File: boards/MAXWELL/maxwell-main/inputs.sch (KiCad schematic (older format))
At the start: 1 part, among them U4 XC7S6-1FTGB196C

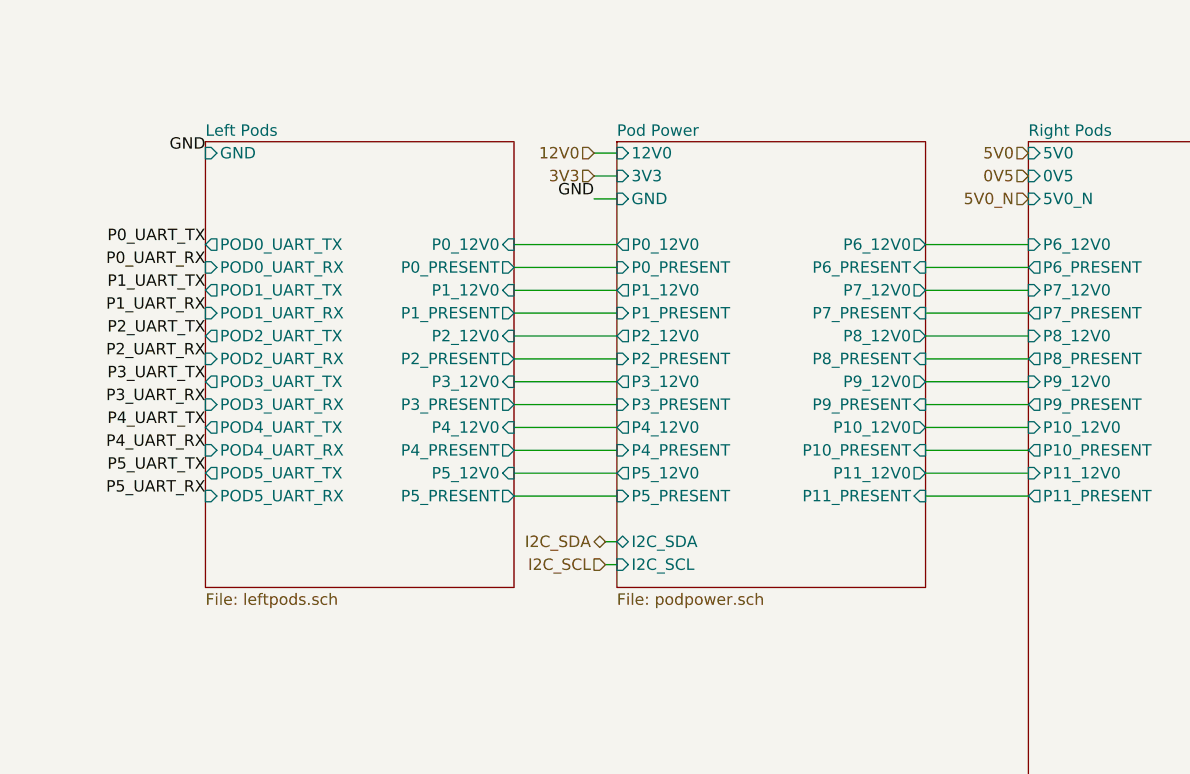
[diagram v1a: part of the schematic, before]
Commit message: Added ferrites to 12V power outputs to improve EMC performance. Fixed incorrect 1V0 hookup for small FPGA. Fixed some other ERC errors
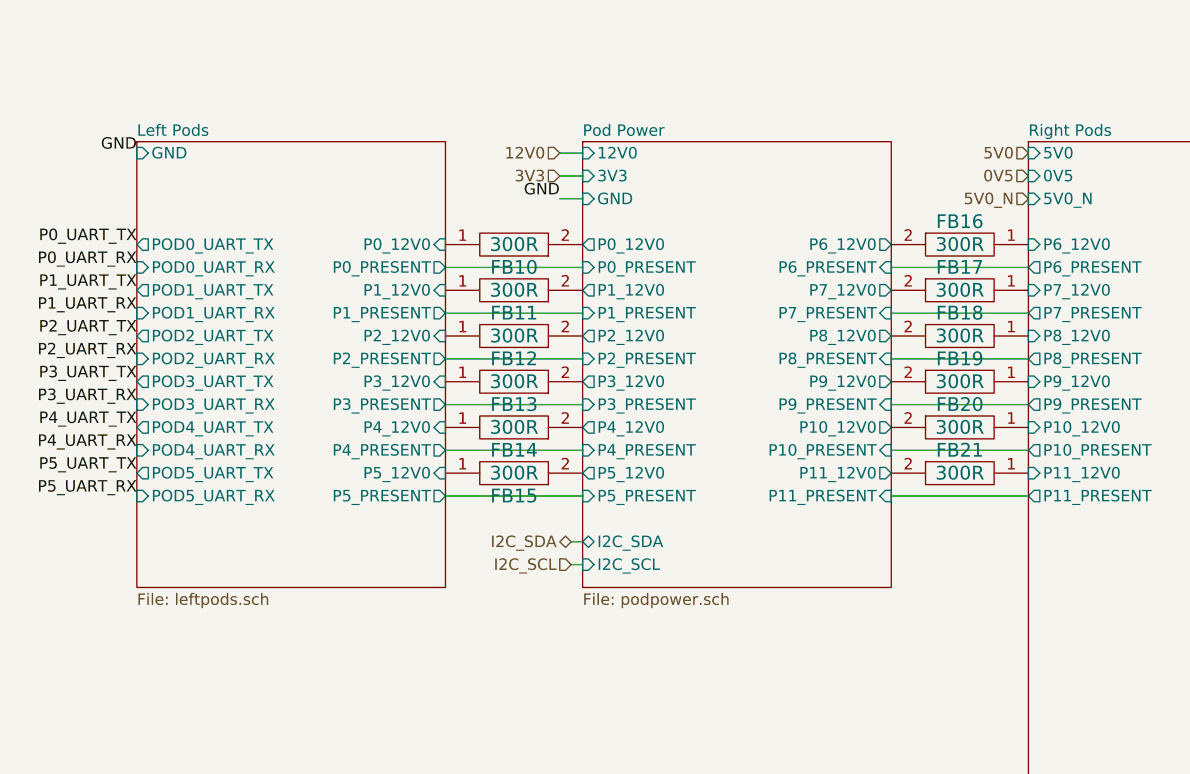
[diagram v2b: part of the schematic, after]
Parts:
- added FB10, FB11, FB12, FB13, FB14, FB15, FB16, FB17, FB18, FB19, FB20, FB21: 300R, symbol passive-azonenberg:FERRITE_SMALL
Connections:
- net Left Pods/P0_12V0: now also FB10.1
- net Left Pods/P1_12V0: now also FB11.1
- net Left Pods/P2_12V0: now also FB12.1
- net Left Pods/P3_12V0: now also FB13.1
- net Left Pods/P4_12V0: now also FB14.1
- net Left Pods/P5_12V0: now also FB15.1
- net Pod Power/P10_12V0: now also FB20.2
- net Pod Power/P11_12V0: now also FB21.2
- net Pod Power/P6_12V0: now also FB16.2
- net Pod Power/P7_12V0: now also FB17.2
- net Pod Power/P8_12V0: now also FB18.2
- net Pod Power/P9_12V0: now also FB19.2
- new net Pod Power/P0_12V0: FB10.2
- new net Pod Power/P1_12V0: FB11.2
- new net Pod Power/P2_12V0: FB12.2
- new net Pod Power/P3_12V0: FB13.2
- new net Pod Power/P4_12V0: FB14.2
- new net Pod Power/P5_12V0: FB15.2
- new net Right Pods/P10_12V0: FB20.1
- new net Right Pods/P11_12V0: FB21.1
- new net Right Pods/P6_12V0: FB16.1
- new net Right Pods/P7_12V0: FB17.1
- new net Right Pods/P8_12V0: FB18.1
- new net Right Pods/P9_12V0: FB19.1

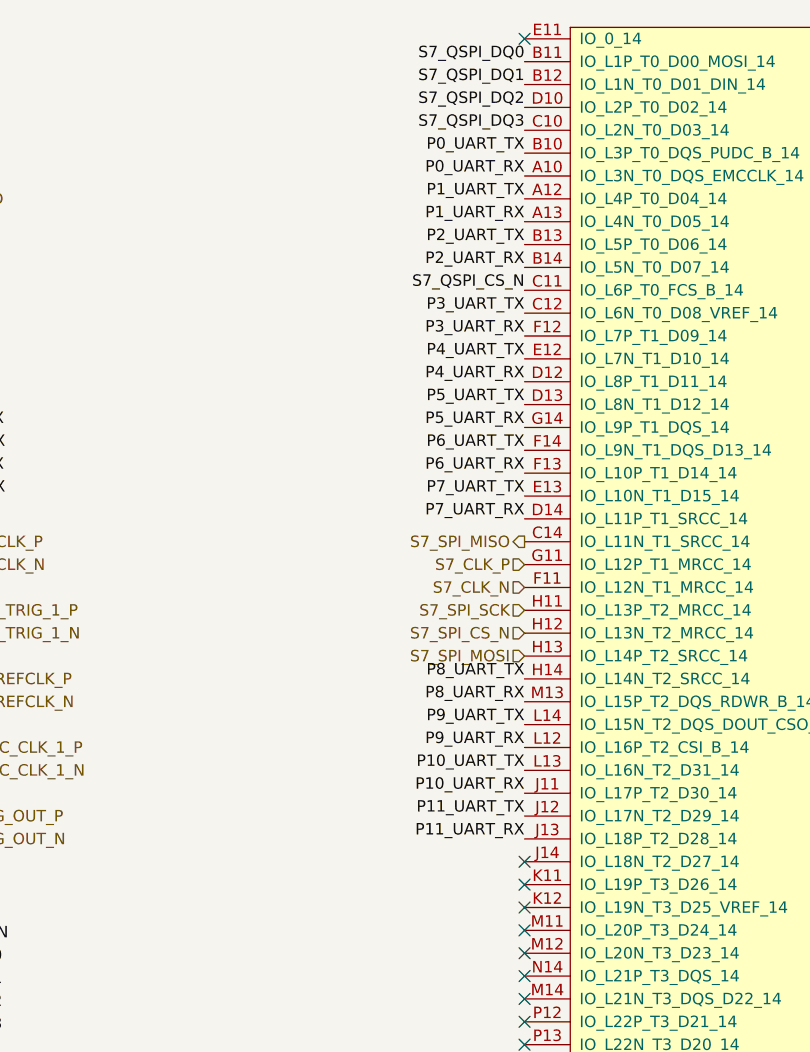
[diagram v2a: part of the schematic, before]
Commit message: Added missing PUDC_B pullup resistors
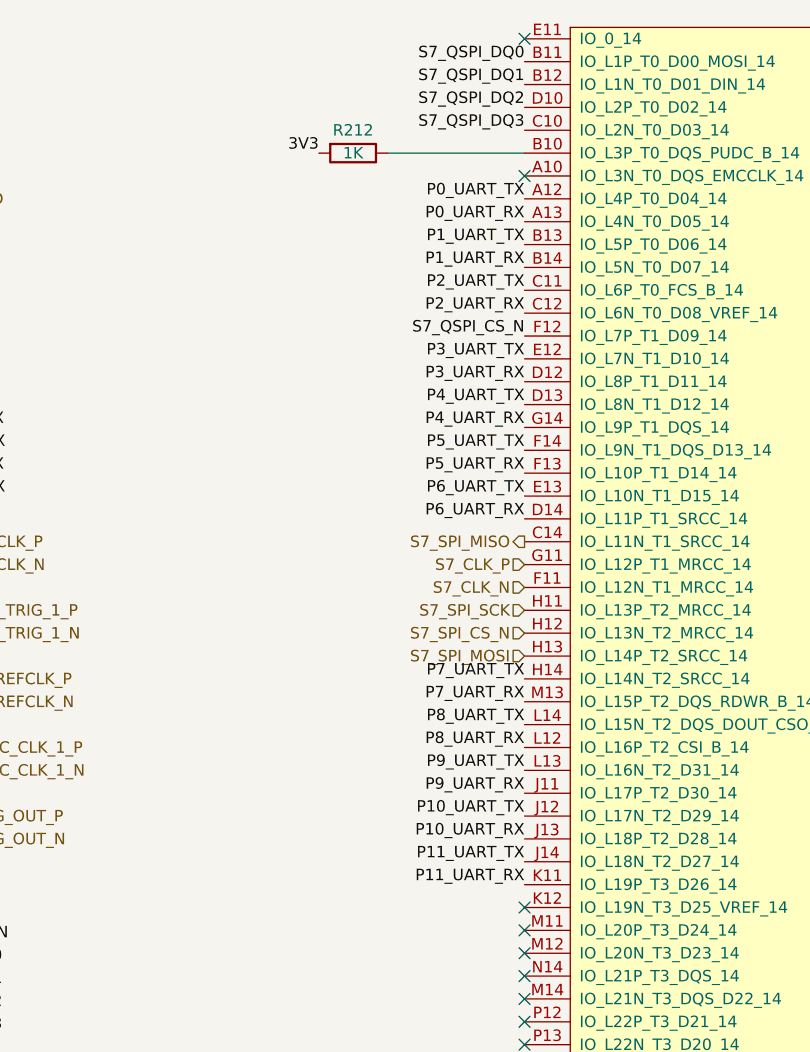
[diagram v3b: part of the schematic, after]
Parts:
- added R212: 1K, symbol device:R
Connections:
- net 3V3: now also R212.2
- net P0_UART_RX: now also U4.A13 (IO_L4N_T0_D05_14); no longer U4.A10 (IO_L3N_T0_DQS_EMCCLK_14)
- net P0_UART_TX: now also U4.A12 (IO_L4P_T0_D04_14); no longer U4.B10 (IO_L3P_T0_DQS_PUDC_B_14)
- net P10_UART_RX: now also U4.J13 (IO_L18P_T2_D28_14); no longer U4.J11 (IO_L17P_T2_D30_14)
- net P10_UART_TX: now also U4.J12 (IO_L17N_T2_D29_14); no longer U4.L13 (IO_L16N_T2_D31_14)
- net P11_UART_RX: now also U4.K11 (IO_L19P_T3_D26_14); no longer U4.J13 (IO_L18P_T2_D28_14)
- net P11_UART_TX: now also U4.J14 (IO_L18N_T2_D27_14); no longer U4.J12 (IO_L17N_T2_D29_14)
- net P1_UART_RX: now also U4.B14 (IO_L5N_T0_D07_14); no longer U4.A13 (IO_L4N_T0_D05_14)
- net P1_UART_TX: now also U4.B13 (IO_L5P_T0_D06_14); no longer U4.A12 (IO_L4P_T0_D04_14)
- net P2_UART_RX: now also U4.C12 (IO_L6N_T0_D08_VREF_14); no longer U4.B14 (IO_L5N_T0_D07_14)
- net P2_UART_TX: now also U4.C11 (IO_L6P_T0_FCS_B_14); no longer U4.B13 (IO_L5P_T0_D06_14)
- net P3_UART_RX: now also U4.D12 (IO_L8P_T1_D11_14); no longer U4.F12 (IO_L7P_T1_D09_14)
- net P3_UART_TX: now also U4.E12 (IO_L7N_T1_D10_14); no longer U4.C12 (IO_L6N_T0_D08_VREF_14)
- net P4_UART_RX: now also U4.G14 (IO_L9P_T1_DQS_14); no longer U4.D12 (IO_L8P_T1_D11_14)
- net P4_UART_TX: now also U4.D13 (IO_L8N_T1_D12_14); no longer U4.E12 (IO_L7N_T1_D10_14)
- net P5_UART_RX: now also U4.F13 (IO_L10P_T1_D14_14); no longer U4.G14 (IO_L9P_T1_DQS_14)
- net P5_UART_TX: now also U4.F14 (IO_L9N_T1_DQS_D13_14); no longer U4.D13 (IO_L8N_T1_D12_14)
- net P6_UART_RX: now also U4.D14 (IO_L11P_T1_SRCC_14); no longer U4.F13 (IO_L10P_T1_D14_14)
- net P6_UART_TX: now also U4.E13 (IO_L10N_T1_D15_14); no longer U4.F14 (IO_L9N_T1_DQS_D13_14)
- net P7_UART_RX: now also U4.M13 (IO_L15P_T2_DQS_RDWR_B_14); no longer U4.D14 (IO_L11P_T1_SRCC_14)
- net P7_UART_TX: now also U4.H14 (IO_L14N_T2_SRCC_14); no longer U4.E13 (IO_L10N_T1_D15_14)
- net P8_UART_RX: now also U4.L12 (IO_L16P_T2_CSI_B_14); no longer U4.M13 (IO_L15P_T2_DQS_RDWR_B_14)
- net P8_UART_TX: now also U4.L14 (IO_L15N_T2_DQS_DOUT_CSO_B_14); no longer U4.H14 (IO_L14N_T2_SRCC_14)
- net P9_UART_RX: now also U4.J11 (IO_L17P_T2_D30_14); no longer U4.L12 (IO_L16P_T2_CSI_B_14)
- net P9_UART_TX: now also U4.L13 (IO_L16N_T2_D31_14); no longer U4.L14 (IO_L15N_T2_DQS_DOUT_CSO_B_14)
- net S7_QSPI_CS_N: now also U4.F12 (IO_L7P_T1_D09_14); no longer U4.C11 (IO_L6P_T0_FCS_B_14)
- new net: R212.1, U4.B10 (IO_L3P_T0_DQS_PUDC_B_14)
- no-connect marks 15 -> 14
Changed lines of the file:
@@
 Sheet 7 18
 Title "MAXWELL Main Board"
-Date "2020-06-21"
+Date "2020-06-22"
 Rev "0.1"
 Comp "Antikernel Labs"
@@
 F13 "S7_DONE" O L 5000 5500 50
 $EndSheet
-Text Label 9100 1950 2    50   ~ 0
+Text Label 9100 2150 2    50   ~ 0
 S7_QSPI_CS_N
 Text Label 9100 950  2    50   ~ 0
@@
 F43 "5V0_N" I L 5000 1550 50
 $EndSheet
-Text Label 9100 1350 2    50   ~ 0
+Text Label 9100 1550 2    50   ~ 0
 P0_UART_TX
-Text Label 9100 1450 2    50   ~ 0
+Text Label 9100 1650 2    50   ~ 0
 P0_UART_RX
 Text HLabel 9100 3150 0    50   Input ~ 0
@@
 Text HLabel 9100 3250 0    50   Input ~ 0
 S7_CLK_N
-Text Label 9100 1550 2    50   ~ 0
+Text Label 9100 1750 2    50   ~ 0
 P1_UART_TX
-Text Label 9100 1650 2    50   ~ 0
+Text Label 9100 1850 2    50   ~ 0
 P1_UART_RX
 Text HLabel 9100 3450 0    50   Input ~ 0
@@
 Text HLabel 9100 3050 0    50   Output ~ 0
 S7_SPI_MISO
-Text Label 9100 1750 2    50   ~ 0
+Text Label 9100 1950 2    50   ~ 0
 P2_UART_TX
-Text Label 9100 1850 2    50   ~ 0
+Text Label 9100 2050 2    50   ~ 0
 P2_UART_RX
-Text Label 9100 2050 2    50   ~ 0
+Text Label 9100 2250 2    50   ~ 0
 P3_UART_TX
-Text Label 9100 2150 2    50   ~ 0
+Text Label 9100 2350 2    50   ~ 0
 P3_UART_RX
-Text Label 9100 2250 2    50   ~ 0
+Text Label 9100 2450 2    50   ~ 0
 P4_UART_TX
-Text Label 9100 2350 2    50   ~ 0
+Text Label 9100 2550 2    50   ~ 0
 P4_UART_RX
-Text Label 9100 2450 2    50   ~ 0
+Text Label 9100 2650 2    50   ~ 0
 P5_UART_TX
-Text Label 9100 2550 2    50   ~ 0
+Text Label 9100 2750 2    50   ~ 0
 P5_UART_RX
-Text Label 9100 2650 2    50   ~ 0
+Text Label 9100 2850 2    50   ~ 0
 P6_UART_TX
-Text Label 9100 2750 2    50   ~ 0
+Text Label 9100 2950 2    50   ~ 0
 P6_UART_RX
-Text Label 9100 2850 2    50   ~ 0
+Text Label 9100 3650 2    50   ~ 0
 P7_UART_TX
-Text Label 9100 2950 2    50   ~ 0
+Text Label 9100 3750 2    50   ~ 0
 P7_UART_RX
-Text Label 9100 3650 2    50   ~ 0
+Text Label 9100 3850 2    50   ~ 0
 P8_UART_TX
-Text Label 9100 3750 2    50   ~ 0
+Text Label 9100 3950 2    50   ~ 0
 P8_UART_RX
-Text Label 9100 3850 2    50   ~ 0
+Text Label 9100 4050 2    50   ~ 0
 P9_UART_TX
-Text Label 9100 3950 2    50   ~ 0
+Text Label 9100 4150 2    50   ~ 0
 P9_UART_RX
-Text Label 9100 4050 2    50   ~ 0
+Text Label 9100 4250 2    50   ~ 0
 P10_UART_TX
-Text Label 9100 4150 2    50   ~ 0
+Text Label 9100 4350 2    50   ~ 0
 P10_UART_RX
-Text Label 9100 4250 2    50   ~ 0
+Text Label 9100 4450 2    50   ~ 0
 P11_UART_TX
-Text Label 9100 4350 2    50   ~ 0
+Text Label 9100 4550 2    50   ~ 0
 P11_UART_RX
 Text HLabel 6600 3050 2    50   Input ~ 0
@@
 NoConn ~ 9100 5750
 NoConn ~ 9100 850
-NoConn ~ 9100 4450
-NoConn ~ 9100 4550
 NoConn ~ 9100 4650
 NoConn ~ 9100 4750
@@
 	-1   0    0    1
 $EndComp
+NoConn ~ 9100 1450
+$Comp
+L device:R R212
+U 1 1 61DE8149
+P 8350 1350
+F 0 "R212" V 8250 1350 50  0000 C CNN
+F 1 "1K" V 8350 1350 50  0000 C CNN
+F 2 "" V 8280 1350 50  0001 C CNN
+F 3 "" H 8350 1350 50  0001 C CNN
+	1    8350 1350
+	0    1    1    0
+$EndComp
+Wire Wire Line
+	8500 1350 9100 1350
+Text Label 8200 1350 2    50   ~ 0
+3V3
 $EndSCHEMATC

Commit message: Continued schematic review. Finished verifying pinouts. Assigned lots more footprints.
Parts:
- FB10, FB11, FB12, FB13, FB14, FB15, FB16, FB17, FB18, FB19, FB20, FB21: footprint (none) -> azonenberg_pcb:EIA_2220_INDUCTOR
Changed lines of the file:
@@
 F 0 "FB11" H 2750 2050 60  0000 C CNN
 F 1 "300R" H 2750 1950 60  0000 C CNN
-F 2 "" H 2750 1950 60  0001 C CNN
+F 2 "azonenberg_pcb:EIA_2220_INDUCTOR" H 2750 1950 60  0001 C CNN
 F 3 "" H 2750 1950 60  0000 C CNN
 	1    2750 1950
@@
 F 0 "FB13" H 2750 2450 60  0000 C CNN
 F 1 "300R" H 2750 2350 60  0000 C CNN
-F 2 "" H 2750 2350 60  0001 C CNN
+F 2 "azonenberg_pcb:EIA_2220_INDUCTOR" H 2750 2350 60  0001 C CNN
 F 3 "" H 2750 2350 60  0000 C CNN
 	1    2750 2350
@@
 F 0 "FB14" H 2750 2650 60  0000 C CNN
 F 1 "300R" H 2750 2550 60  0000 C CNN
-F 2 "" H 2750 2550 60  0001 C CNN
+F 2 "azonenberg_pcb:EIA_2220_INDUCTOR" H 2750 2550 60  0001 C CNN
 F 3 "" H 2750 2550 60  0000 C CNN
 	1    2750 2550
@@
 F 0 "FB15" H 2750 2850 60  0000 C CNN
 F 1 "300R" H 2750 2750 60  0000 C CNN
-F 2 "" H 2750 2750 60  0001 C CNN
+F 2 "azonenberg_pcb:EIA_2220_INDUCTOR" H 2750 2750 60  0001 C CNN
 F 3 "" H 2750 2750 60  0000 C CNN
 	1    2750 2750
@@
 F 0 "FB16" H 4700 1850 60  0000 C CNN
 F 1 "300R" H 4700 1750 60  0000 C CNN
-F 2 "" H 4700 1750 60  0001 C CNN
+F 2 "azonenberg_pcb:EIA_2220_INDUCTOR" H 4700 1750 60  0001 C CNN
 F 3 "" H 4700 1750 60  0000 C CNN
 	1    4700 1750
@@
 F 0 "FB17" H 4700 2050 60  0000 C CNN
 F 1 "300R" H 4700 1950 60  0000 C CNN
-F 2 "" H 4700 1950 60  0001 C CNN
+F 2 "azonenberg_pcb:EIA_2220_INDUCTOR" H 4700 1950 60  0001 C CNN
 F 3 "" H 4700 1950 60  0000 C CNN
 	1    4700 1950
@@
 F 0 "FB18" H 4700 2250 60  0000 C CNN
 F 1 "300R" H 4700 2150 60  0000 C CNN
-F 2 "" H 4700 2150 60  0001 C CNN
+F 2 "azonenberg_pcb:EIA_2220_INDUCTOR" H 4700 2150 60  0001 C CNN
 F 3 "" H 4700 2150 60  0000 C CNN
 	1    4700 2150
@@
 F 0 "FB19" H 4700 2450 60  0000 C CNN
 F 1 "300R" H 4700 2350 60  0000 C CNN
-F 2 "" H 4700 2350 60  0001 C CNN
+F 2 "azonenberg_pcb:EIA_2220_INDUCTOR" H 4700 2350 60  0001 C CNN
 F 3 "" H 4700 2350 60  0000 C CNN
 	1    4700 2350
@@
 F 0 "FB20" H 4700 2650 60  0000 C CNN
 F 1 "300R" H 4700 2550 60  0000 C CNN
-F 2 "" H 4700 2550 60  0001 C CNN
+F 2 "azonenberg_pcb:EIA_2220_INDUCTOR" H 4700 2550 60  0001 C CNN
 F 3 "" H 4700 2550 60  0000 C CNN
 	1    4700 2550
@@
 F 0 "FB21" H 4700 2850 60  0000 C CNN
 F 1 "300R" H 4700 2750 60  0000 C CNN
-F 2 "" H 4700 2750 60  0001 C CNN
+F 2 "azonenberg_pcb:EIA_2220_INDUCTOR" H 4700 2750 60  0001 C CNN
 F 3 "" H 4700 2750 60  0000 C CNN
 	1    4700 2750
@@
 F 0 "FB10" H 2750 1850 60  0000 C CNN
 F 1 "300R" H 2750 1750 60  0000 C CNN
-F 2 "" H 2750 1750 60  0001 C CNN
+F 2 "azonenberg_pcb:EIA_2220_INDUCTOR" H 2750 1750 60  0001 C CNN
 F 3 "" H 2750 1750 60  0000 C CNN
 	1    2750 1750
@@
 F 0 "FB12" H 2750 2250 60  0000 C CNN
 F 1 "300R" H 2750 2150 60  0000 C CNN
-F 2 "" H 2750 2150 60  0001 C CNN
+F 2 "azonenberg_pcb:EIA_2220_INDUCTOR" H 2750 2150 60  0001 C CNN
 F 3 "" H 2750 2150 60  0000 C CNN
 	1    2750 2150

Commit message: Assigned footprints for all resistors
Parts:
- R212: footprint (none) -> azonenberg_pcb:EIA_0402_RES_NOSILK
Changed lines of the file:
@@
 Sheet 7 18
 Title "MAXWELL Main Board"
-Date "2020-06-22"
+Date "2020-06-23"
 Rev "0.1"
 Comp "Antikernel Labs"
@@
 F 0 "R212" V 8250 1350 50  0000 C CNN
 F 1 "1K" V 8350 1350 50  0000 C CNN
-F 2 "" V 8280 1350 50  0001 C CNN
+F 2 "azonenberg_pcb:EIA_0402_RES_NOSILK" V 8280 1350 50  0001 C CNN
 F 3 "" H 8350 1350 50  0001 C CNN
 	1    8350 1350

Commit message: Added footprints for most ICs other than DC-DC modules
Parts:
- U4: footprint (none) -> azonenberg_pcb:BGA_196_15x15_FULLARRAY_1MM_FTGB196
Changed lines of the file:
@@
 F 0 "U4" H 9300 5750 50  0000 L CNN
 F 1 "XC7S6-1FTGB196C" H 9300 5650 50  0000 L CNN
-F 2 "" H 9300 5800 50  0001 C CNN
+F 2 "azonenberg_pcb:BGA_196_15x15_FULLARRAY_1MM_FTGB196" H 9300 5800 50  0001 C CNN
 F 3 "" H 9300 5800 50  0001 C CNN
 	3    9300 5800
